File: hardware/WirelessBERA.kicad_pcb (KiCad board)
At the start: 4 copper layers, 73 x 94 mm, 187 parts, among them J1 Conn_01x02, J2 Micro_SD_Card, J3 USB_C_Receptacle, J4 AudioJack3, J5 AudioJack3, SW1 SW_SPDT, SW2 SW_Push, SW3 SW_Push, U1 TPS7A2033PDBVR, U10 LTC6373, U11 TAC5212, U2 BQ24074RGT, U3 TPS7A94, U4 TPS7A39, U5 TPS65132W, U6 TPS63000, U7 ESP32-S3-WROOM-1, U8 WE-TVS-82400102, U9 OPA376xxDBV

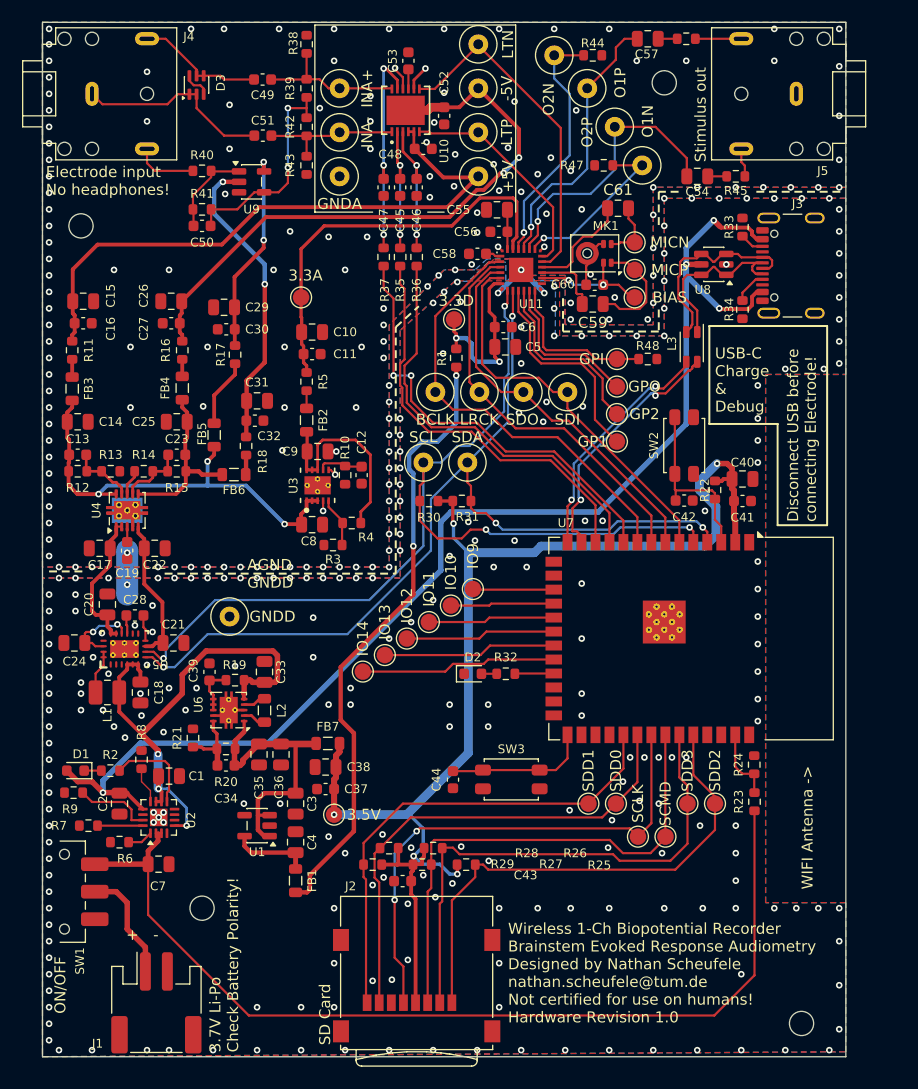
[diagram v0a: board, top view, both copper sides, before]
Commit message: Changed Pinheader and found a Problem with V0CM.
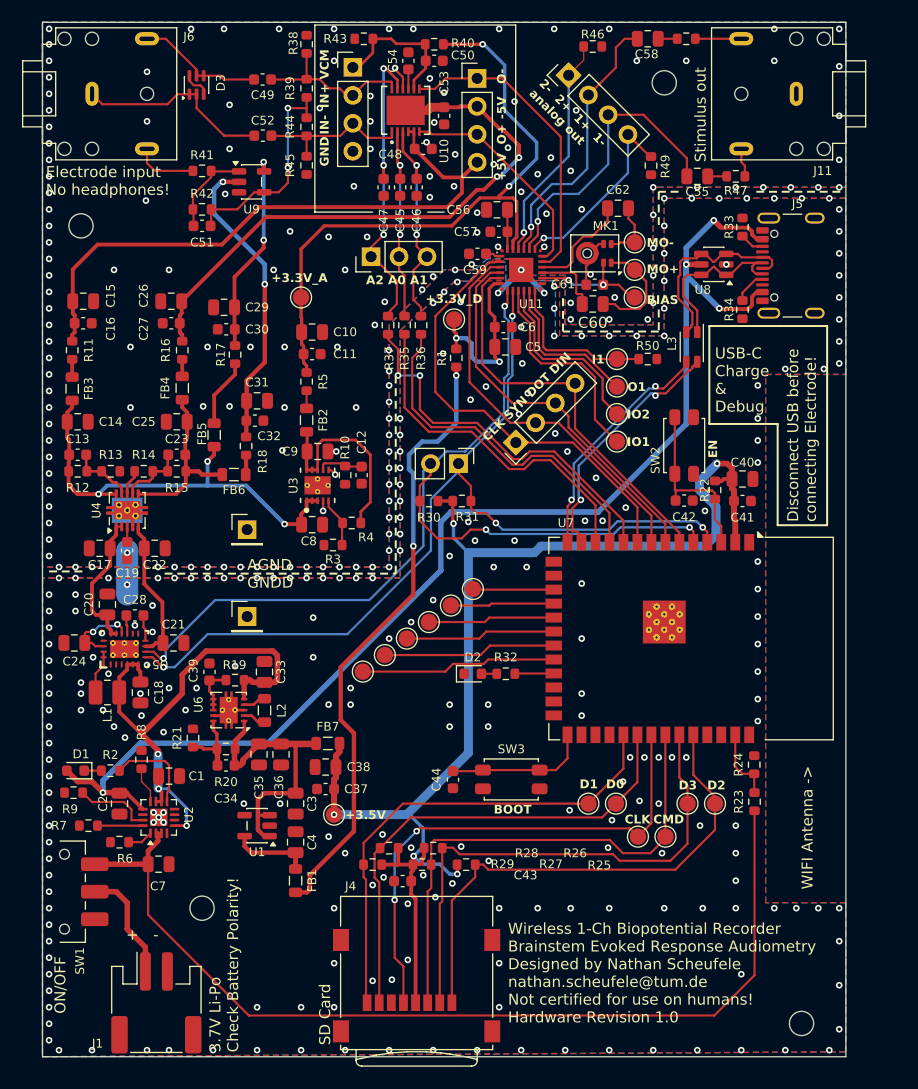
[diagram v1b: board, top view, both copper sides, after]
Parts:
- removed the TP20 at (55.5, 42.5)
- removed the TP21 at (68.1, 46.5)
- removed the TP22 at (68.1, 38.5)
- removed TP23, TP24, TP25, TP26, TP27, TP28, TP29, TP31, TP32, TP35, TP40: TestPoint_Small, TestPoint:TestPoint_Loop_D2.60mm_Drill0.9mm_Beaded
- removed the TP3 at (45.5, 90.5)
- removed the TP4 at (68.1, 50.5)
- removed the TP5 at (68.1, 42.5)
- removed the TP7 at (55.5, 50.5)
- added C50: 1u, Capacitor_SMD:C_0603_1608Metric, F.Cu at (64.1, 40.0)
- added J10: PinHeader_01x04_2.54mm_Vertical, Connector_PinHeader_2.54mm:PinHeader_1x04_P2.54mm_Vertical, F.Cu at (76.3, 41.3)
- added J12: PinHeader_01x04_2.54mm_Vertical, Connector_PinHeader_2.54mm:PinHeader_1x04_P2.54mm_Vertical, F.Cu at (71.5, 74.7)
- added J13: PinHeader_01x02_2.54mm_Vertical, Connector_PinHeader_2.54mm:PinHeader_1x02_P2.54mm_Vertical, F.Cu at (66.3, 76.6)
- added J2: PinHeader_01x01_2.54mm_Vertical, Connector_PinHeader_2.54mm:PinHeader_1x01_P2.54mm_Vertical, F.Cu at (47.1, 90.5)
- added J3: PinHeader_01x01_2.54mm_Vertical, Connector_PinHeader_2.54mm:PinHeader_1x01_P2.54mm_Vertical, F.Cu at (47.1, 82.6)
- added J7: PinHeader_01x04_2.54mm_Vertical, Connector_PinHeader_2.54mm:PinHeader_1x04_P2.54mm_Vertical, F.Cu at (68.0, 41.6)
- added J8: PinHeader_01x04_2.54mm_Vertical, Connector_PinHeader_2.54mm:PinHeader_1x04_P2.54mm_Vertical, F.Cu at (56.7, 40.6)
- added J9: PinHeader_01x03_2.54mm_Vertical, Connector_PinHeader_2.54mm:PinHeader_1x03_P2.54mm_Vertical, F.Cu at (58.4, 57.8)
- added R40: 5k, Resistor_SMD:R_0603_1608Metric, F.Cu at (64.1, 38.5)
- added R43: 10k, Resistor_SMD:R_0603_1608Metric, F.Cu at (57.7, 38.0)
- moved R35 6.21 mm to (61.4, 64.0)
- moved R36 6.21 mm to (62.9, 64.0)
- moved R37 6.21 mm to (59.9, 64.0)
- moved R49 4.30 mm to (83.8, 49.5), turned to -90 degrees
- moved R46 0.80 mm to (78.5, 38.7)
- renumbered C50 to C51, C51 to C52, C52 to C53, C53 to C54, C54 to C55, C55 to C56, C56 to C57, C57 to C58, C58 to C59, C59 to C60, C60 to C61, C61 to C62, J5 to J11, J2 to J4, J3 to J5, J4 to J6, R40 to R41, R41 to R42, R42 to R44, R43 to R45, R44 to R46, R45 to R47, R46 to R48, R47 to R49, R48 to R50, TP14 to TP10, TP15 to TP11, TP16 to TP12, TP17 to TP13, TP18 to TP14, TP19 to TP15, TP30 to TP16, TP33 to TP17, TP34 to TP18, TP36 to TP19, TP37 to TP20, TP38 to TP21, TP39 to TP22, TP6 to TP3, TP8 to TP4, TP9 to TP5, TP10 to TP6, TP11 to TP7, TP12 to TP8, TP13 to TP9
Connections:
- net Net-(U10-IN+) renamed /Analog/IN+
- net Net-(U10-IN-) renamed /Analog/IN-
- U10 pad 8: GNDA -> /Analog/V0CM
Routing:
- net +3.3V_TAC_A: track 37.5 -> 58.6 mm, vias 0 -> 2
- net /Analog/V0CM: track 0.00 -> 13.1 mm
- net /Analog/A2: track 20.0 -> 28.1 mm
- net /Analog/A1: track 12.3 -> 19.7 mm
- net /Analog/A0: track 11.9 -> 18.3 mm
- net GAIN_A0: track 37.7 -> 31.7 mm
- net GAIN_A1: track 38.2 -> 32.2 mm
- net GAIN_A2: track 40.0 -> 34.4 mm
- net /Analog/LTC6373_OUT_N: track 30.8 -> 27.9 mm
- net GNDA: track 23.1 -> 20.8 mm, vias 161 -> 164
- net -5V_InAmp: track 55.1 -> 52.9 mm
- net /Analog/OUT_1_N: track 15.7 -> 17.9 mm
- net /Analog/OUT_2_N: track 22.8 -> 20.9 mm
- net /Analog/IN-: track 13.0 -> 14.4 mm
- net /Analog/IN+: track 13.7 -> 15.1 mm
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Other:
- board text added: "+3.3V_A"
- board text added: "+3.3V_D"
- board text added: "+3.5V"
- board text added: "+5V"
- board text added: "-5V"
- board text added: "2- 2+ 1+ 1- analog out"
- board text added: "A2 A0 A1"
- board text added: "BIAS"
- board text added: "BOOT"
- board text added: "CLK"
- board text added: "CLK SYN DOT DIN"
- board text added: "CMD"
- board text added: "D0"
- board text added: "D1"
- board text added: "D2"
- board text added: "D3"
- board text added: "EN"
- board text added: "GND"
- board text added: "I1"
- board text added: "IN+"
- board text added: "IN-"
- board text added: "IO1"
- board text added: "IO2"
- board text added: "MO+"
- board text added: "MO-"
- board text added: "O+"
- board text added: "O-"
- board text added: "O1"
- board text added: "VCM"

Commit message: Release: First PCB manufacturing batch. Fixed U10 thermal via short, exempted fiducials from solder mask margin override rule, adjusted R22 label, and updated all manufacturing files.
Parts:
- added FID1: Fiducial, Fiducial:Fiducial_0.5mm_Mask1mm, F.Cu at (90.0, 115.0)
- added FID2: Fiducial, Fiducial:Fiducial_0.5mm_Mask1mm, F.Cu at (50.0, 120.0)
- added FID3: Fiducial, Fiducial:Fiducial_0.5mm_Mask1mm, F.Cu at (36.0, 55.0)
- R40: value 5k -> 4.99k
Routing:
- net -5V_InAmp: vias 2 -> 8
- added copper zone on B.Cu, net -5V_InAmp
